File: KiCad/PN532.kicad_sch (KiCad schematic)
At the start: 56 parts, among them J1 Bell, J2 Header, J3 SPOX, SW1 TAMPER, U1 PN532, U2 QR, U3 QR, Y1 27.12MHz

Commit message: More cut down.
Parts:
- removed J2: Header, RevK:PinHeader_1x04_P2.54mm_Vertical, symbol Connector:Conn_01x04_Male
- J3: footprint RevK:Molex_MiniSPOX_H4RA -> RevK:Molex_MiniSPOX_H4V
- SW1: footprint RevK:SW_PUSH_6mm_PTH_SMD -> RevK:SW_PUSH_6mm_SMD
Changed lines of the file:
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@@
   (junction (at 123.19 50.8) (diameter 0) (color 0 0 0 0)
   )
-  (junction (at 265.43 83.82) (diameter 0) (color 0 0 0 0)
-  )
   (junction (at 85.09 92.71) (diameter 0) (color 0 0 0 0)
   )
@@
   )
   (junction (at 132.08 50.8) (diameter 0) (color 0 0 0 0)
-  )
-  (junction (at 262.89 81.28) (diameter 0) (color 0 0 0 0)
   )
   (junction (at 154.94 161.29) (diameter 0) (color 0 0 0 0)
@@
     (stroke (width 0) (type default) (color 0 0 0 0))
   )
-  (wire (pts (xy 252.73 64.77) (xy 262.89 64.77))
-    (stroke (width 0) (type default) (color 0 0 0 0))
-  )
   (wire (pts (xy 158.75 139.7) (xy 146.05 139.7))
     (stroke (width 0) (type default) (color 0 0 0 0))
@@
     (stroke (width 0) (type default) (color 0 0 0 0))
   )
-  (wire (pts (xy 252.73 67.31) (xy 265.43 67.31))
-    (stroke (width 0) (type default) (color 0 0 0 0))
-  )
   (wire (pts (xy 67.31 102.87) (xy 85.09 102.87))
     (stroke (width 0) (type default) (color 0 0 0 0))
@@
     (stroke (width 0) (type default) (color 0 0 0 0))
   )
-  (wire (pts (xy 265.43 67.31) (xy 265.43 83.82))
-    (stroke (width 0) (type default) (color 0 0 0 0))
-  )
   (wire (pts (xy 209.55 62.23) (xy 203.2 62.23))
     (stroke (width 0) (type default) (color 0 0 0 0))
@@
     (stroke (width 0) (type default) (color 0 0 0 0))
   )
-  (wire (pts (xy 262.89 64.77) (xy 262.89 81.28))
-    (stroke (width 0) (type default) (color 0 0 0 0))
-  )
   (wire (pts (xy 110.49 85.09) (xy 119.38 85.09))
     (stroke (width 0) (type default) (color 0 0 0 0))
@@
   )
   (text "GND\nVCC\nTX\nRX" (at 242.57 82.55 0)
-    (effects (font (size 1.27 1.27)) (justify left bottom))
-  )
-  (text "GND\nVCC\nTX\nRX" (at 242.57 67.31 0)
     (effects (font (size 1.27 1.27)) (justify left bottom))
   )
@@
     (property "Reference" "SW1" (id 0) (at 209.55 13.081 0))
     (property "Value" "TAMPER" (id 1) (at 209.55 15.3924 0))
-    (property "Footprint" "RevK:SW_PUSH_6mm_PTH_SMD" (id 2) (at 209.55 15.24 0)
+    (property "Footprint" "RevK:SW_PUSH_6mm_SMD" (id 2) (at 209.55 15.24 0)
       (effects (font (size 1.27 1.27)) hide)
     )
@@
     (pin "1")
   )
-  (symbol (lib_id "Connector:Conn_01x04_Male") (at 247.65 62.23 0) (unit 1)
-    (in_bom no) (on_board yes)
-    (property "Reference" "J2" (id 0) (at 250.3932 55.0926 0))
-    (property "Value" "Header" (id 1) (at 250.3932 57.404 0))
-    (property "Footprint" "RevK:PinHeader_1x04_P2.54mm_Vertical" (id 2) (at 247.65 62.23 0)
-      (effects (font (size 1.27 1.27)) hide)
-    )
-    (property "Datasheet" "~" (id 3) (at 247.65 62.23 0)
-      (effects (font (size 1.27 1.27)) hide)
-    )
-    (property "Note" "Non fit" (id 4) (at 247.65 62.23 0)
-      (effects (font (size 1.27 1.27)) hide)
-    )
-    (pin "1")
-    (pin "2")
-    (pin "3")
-    (pin "4")
-  )
   (symbol (lib_id "Connector:Conn_01x04_Male") (at 247.65 78.74 0) (unit 1)
     (in_bom no) (on_board yes)
     (property "Reference" "J3" (id 0) (at 250.3932 71.6026 0))
     (property "Value" "SPOX" (id 1) (at 250.3932 73.914 0))
-    (property "Footprint" "RevK:Molex_MiniSPOX_H4RA" (id 2) (at 247.65 78.74 0)
+    (property "Footprint" "RevK:Molex_MiniSPOX_H4V" (id 2) (at 247.65 78.74 0)
       (effects (font (size 1.27 1.27)) hide)
     )
@@
     (pin "4")
   )
-  (symbol (lib_id "power:GND") (at 252.73 59.69 90) (unit 1)
-    (in_bom yes) (on_board yes)
-    (property "Reference" "#PWR041" (id 0) (at 259.08 59.69 0)
-      (effects (font (size 1.27 1.27)) hide)
-    )
-    (property "Value" "GND" (id 1) (at 255.9812 59.563 90)
-      (effects (font (size 1.27 1.27)) (justify right))
-    )
-    (property "Footprint" "" (id 2) (at 252.73 59.69 0)
-      (effects (font (size 1.27 1.27)) hide)
-    )
-    (property "Datasheet" "" (id 3) (at 252.73 59.69 0)
-      (effects (font (size 1.27 1.27)) hide)
-    )
-    (pin "1")
-  )
   (symbol (lib_id "power:GND") (at 252.73 76.2 90) (unit 1)
     (in_bom yes) (on_board yes)
@@
     )
     (property "Datasheet" "" (id 3) (at 252.73 76.2 0)
-      (effects (font (size 1.27 1.27)) hide)
-    )
-    (pin "1")
-  )
-  (symbol (lib_id "power:+5V") (at 252.73 62.23 270) (unit 1)
-    (in_bom no) (on_board yes)
-    (property "Reference" "#PWR042" (id 0) (at 248.92 62.23 0)
-      (effects (font (size 1.27 1.27)) hide)
-    )
-    (property "Value" "+5V" (id 1) (at 255.9812 62.611 90)
-      (effects (font (size 1.27 1.27)) (justify left))
-    )
-    (property "Footprint" "" (id 2) (at 252.73 62.23 0)
-      (effects (font (size 1.27 1.27)) hide)
-    )
-    (property "Datasheet" "" (id 3) (at 252.73 62.23 0)
       (effects (font (size 1.27 1.27)) hide)
     )
@@
       (reference "#PWR040") (unit 1) (value "GND") (footprint "")
     )
-    (path "/00000000-0000-0000-0000-0000607d87e0"
-      (reference "#PWR041") (unit 1) (value "GND") (footprint "")
-    )
-    (path "/00000000-0000-0000-0000-0000607d9eea"
-      (reference "#PWR042") (unit 1) (value "+5V") (footprint "")
-    )
     (path "/00000000-0000-0000-0000-0000607d93e3"
       (reference "#PWR043") (unit 1) (value "GND") (footprint "")
@@
       (reference "J1") (unit 1) (value "Bell") (footprint "RevK:PinHeader_1x02_P2.54mm_Vertical")
     )
-    (path "/00000000-0000-0000-0000-0000607d09fb"
-      (reference "J2") (unit 1) (value "Header") (footprint "RevK:PinHeader_1x04_P2.54mm_Vertical")
-    )
     (path "/00000000-0000-0000-0000-0000607d486c"
-      (reference "J3") (unit 1) (value "SPOX") (footprint "RevK:Molex_MiniSPOX_H4RA")
+      (reference "J3") (unit 1) (value "SPOX") (footprint "RevK:Molex_MiniSPOX_H4V")
     )
     (path "/00000000-0000-0000-0000-0000609405db"
@@
     )
     (path "/00000000-0000-0000-0000-00006076e91e"
-      (reference "SW1") (unit 1) (value "TAMPER") (footprint "RevK:SW_PUSH_6mm_PTH_SMD")
+      (reference "SW1") (unit 1) (value "TAMPER") (footprint "RevK:SW_PUSH_6mm_SMD")
     )
     (path "/00000000-0000-0000-0000-0000609b72f2"

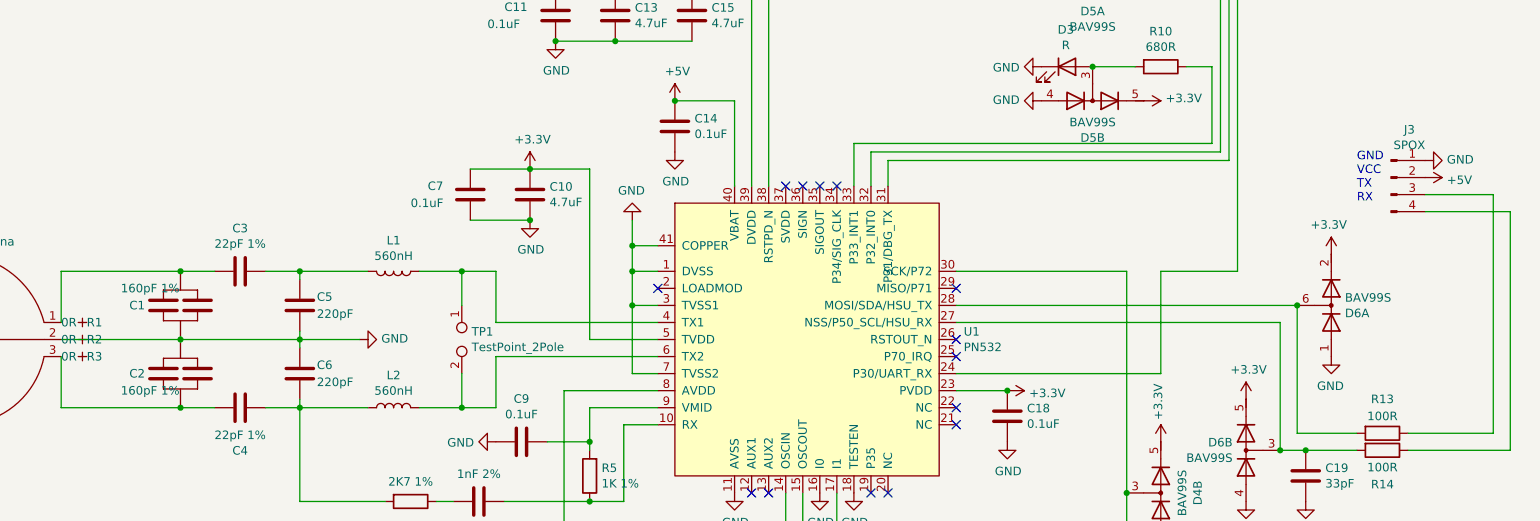
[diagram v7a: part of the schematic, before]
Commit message: Cleaner up BOM
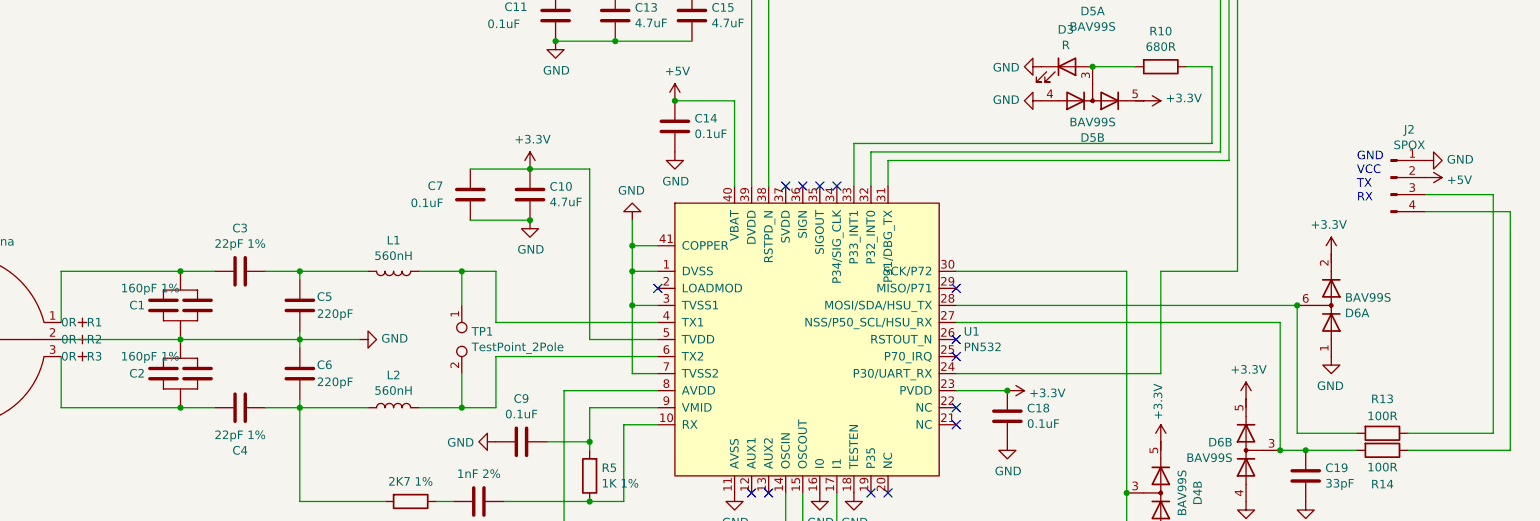
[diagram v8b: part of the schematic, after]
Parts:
- C1, C2: Manufacturer (none) -> KEMET; Part No (none) -> C0603X161F1HACTU
- C10, C13, C15: Manufacturer (none) -> Samsung Electro-Mechanics; Part No (none) -> CL10A475KP8NNNC
- C11, C12, C18, C7, C9: Manufacturer (none) -> KEMET; Part No (none) -> C0603C104M4RACTU
- C16, C17, C3, C4: Manufacturer (none) -> Walsin; Part No (none) -> 0603N220F500CT
- C19: Manufacturer (none) -> KEMET; Part No (none) -> C0603C330G8HACTU
- C5, C6: Manufacturer (none) -> Vishay / Vitramon; Part No (none) -> VJ0603A221GXAPW1BC
- C8: Manufacturer (none) -> Vishay / Vitramon; Part No (none) -> VJ0603A102GXAPW1BC
- D1: Manufacturer (none) -> Kingbright; Part No (none) -> APTD1608LCGCK
- D2: Manufacturer (none) -> Kingbright; Part No (none) -> APHD1608LSYCK
- D3: Manufacturer (none) -> Kingbright; Part No (none) -> APHD1608LSURCK
- D4, D5, D6: Manufacturer (none) -> Nexperia; Part No (none) -> BAV99S,115
- L1, L2: Manufacturer (none) -> Murata Electronics; Part No (none) -> LQW2UASR56G00L
- R1, R3: Manufacturer (none) -> Bourns; Part No (none) -> CR0603-J/-000ELF
- R10: Manufacturer (none) -> YAGE; Part No (none) -> RC0603JR-07680RL
- R11, R15, R6: Manufacturer (none) -> Bourns; Part No (none) -> CR0603-FX-1002ELF
- R12, R13, R14: Manufacturer (none) -> YAGEO; Part No (none) -> RC0603JR-07100RL
- R2, R4: Manufacturer (none) -> YAGEO; Part No (none) -> RC0603FR-102K7L
- R5: Manufacturer (none) -> Vishay / Dale; Part No (none) -> CRCW06031K00FKEAC
- R7: Manufacturer (none) -> YAGEO; Part No (none) -> RC0603JR-1020KL
- R8: Manufacturer (none) -> YAGEO; Part No (none) -> AC0603JR-07470RL
- R9: Manufacturer (none) -> YAGEO; Part No (none) -> RC0603JR-07680RL
- SW1: Manufacturer (none) -> E-Switch; Part No (none) -> LL3301NF065QG
- U1: Manufacturer (none) -> NXP Semiconductors; Part No (none) -> PN5321A3HN/C106,51
- Y1: Manufacturer (none) -> Wurth Elektronik; Part No (none) -> 830053099
- renumbered J3 to J2
